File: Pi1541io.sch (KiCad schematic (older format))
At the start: 19 parts, among them J1 IEC, J2 IEC2, J3 ExtSpkr, P1 Conn_02x20_Odd_Even, SW1 SW_Push, SW2 SW_Push, SW3 SW_Push, SW4 SW_Push, SW5 SW_Push, U1 LevelShifter

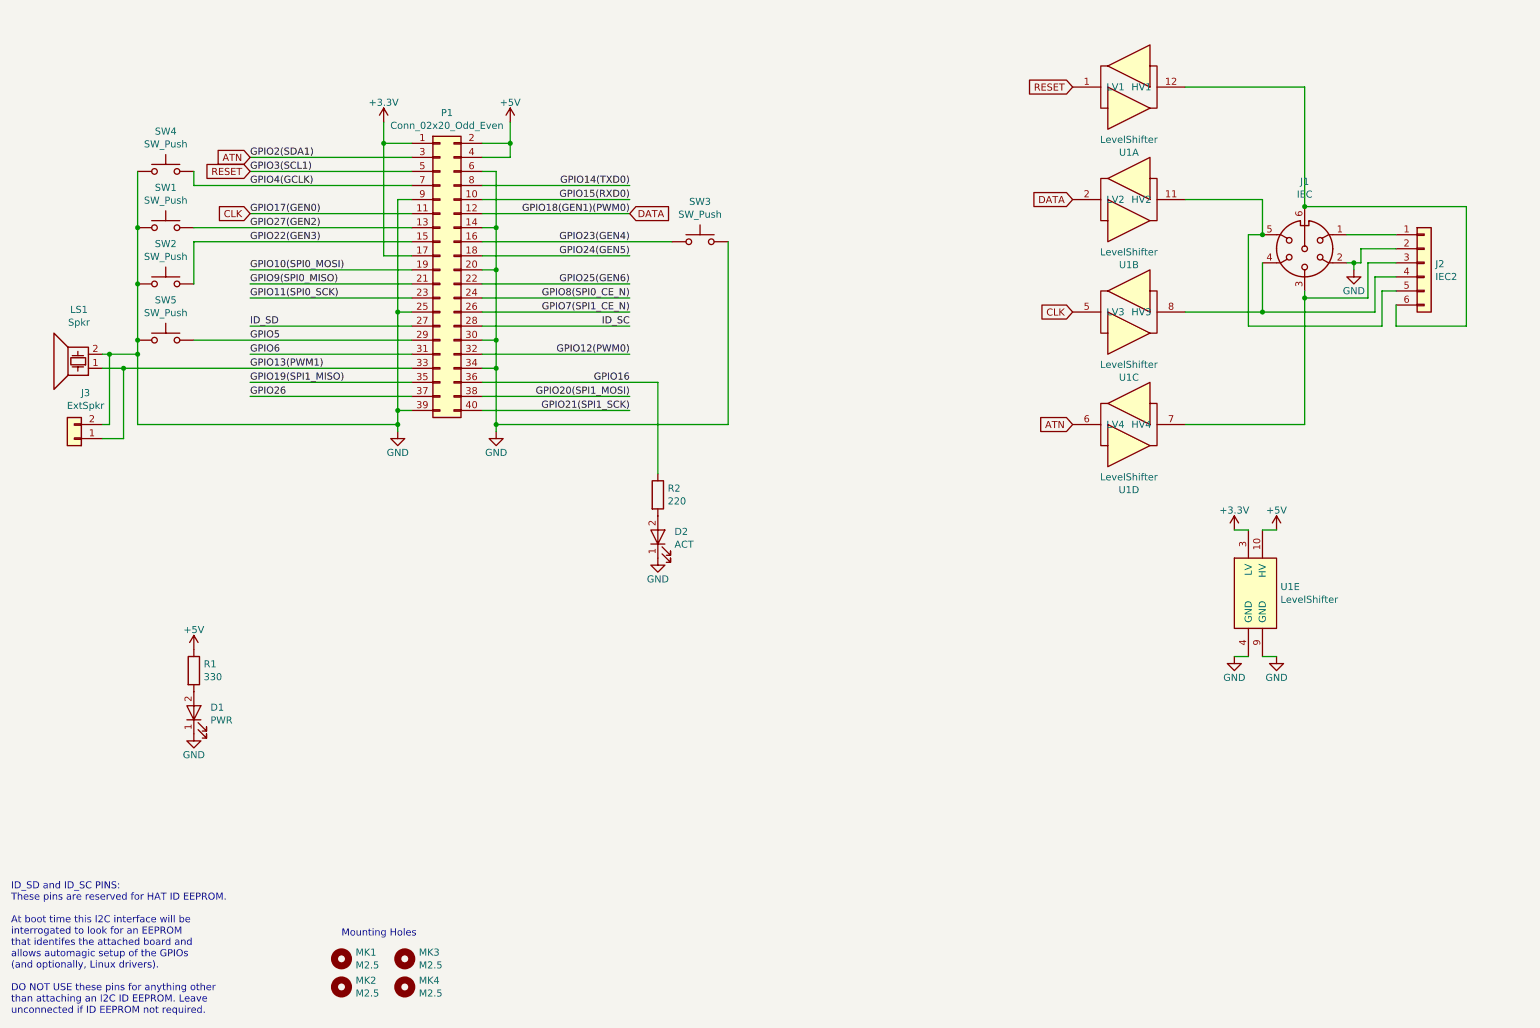
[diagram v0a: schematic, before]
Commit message: Added second IEC port and reset button.
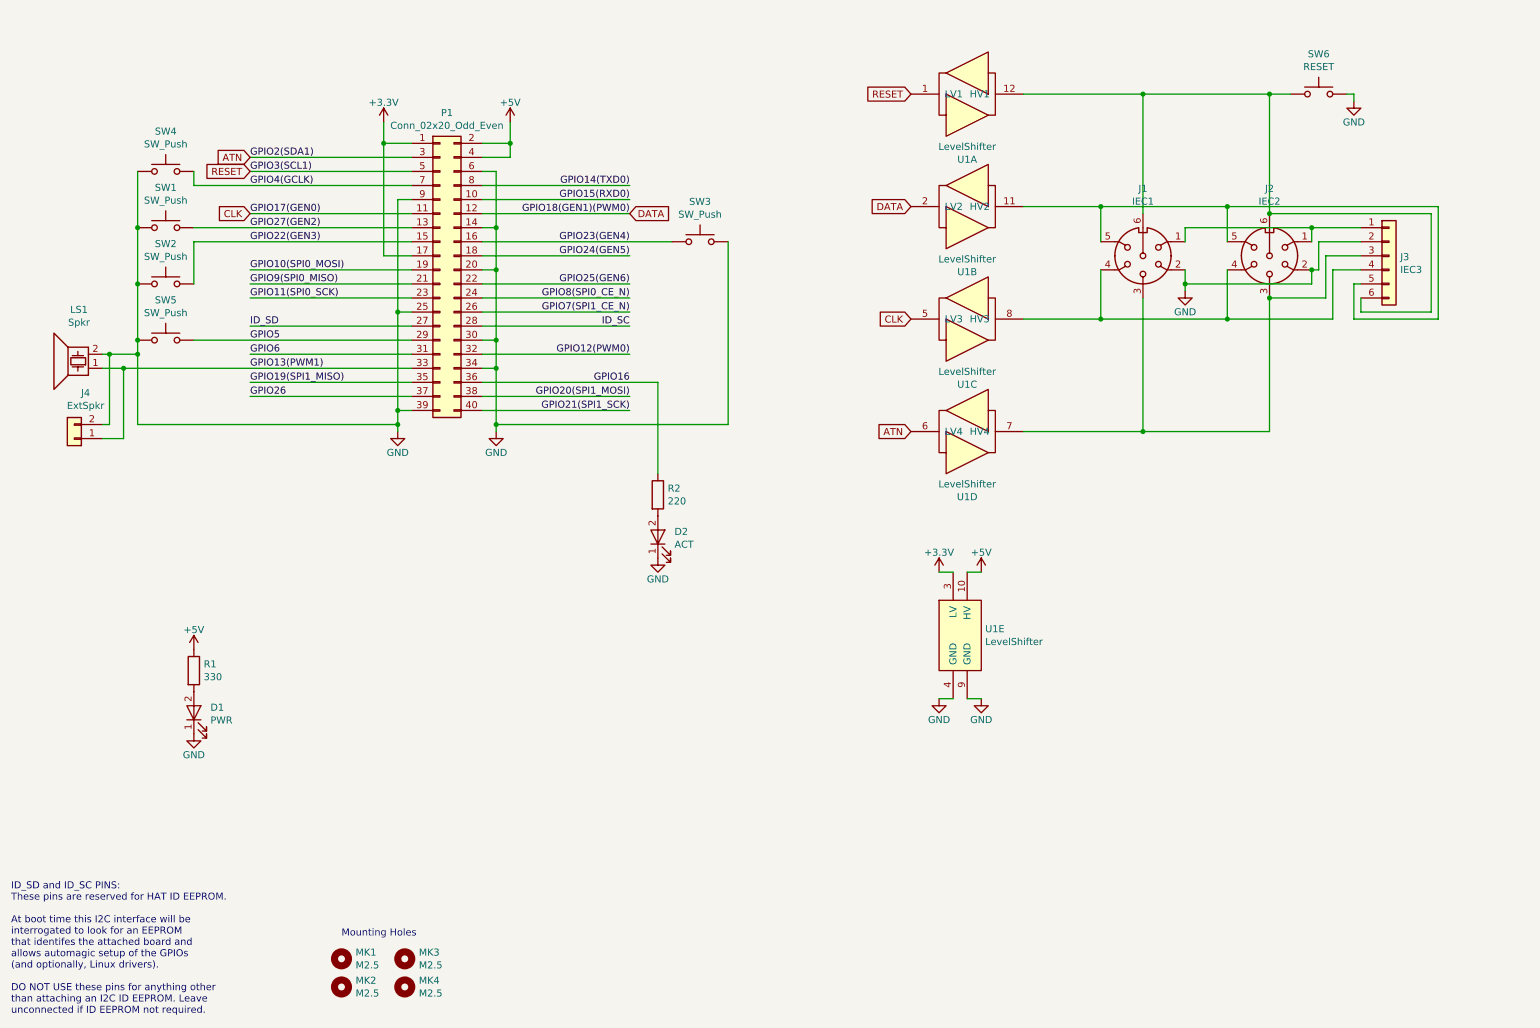
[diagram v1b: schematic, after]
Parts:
- added J2: IEC2, DIN-Connector:DIN-6, symbol Connector:DIN-6
- added SW6: RESET, Buttons_Switches_THT:SW_PUSH_6mm, symbol Switch:SW_Push
- J1: value IEC -> IEC1
- J3: renamed from J2; value IEC2 -> IEC3
- renumbered J3 to J4
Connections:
- net GND: now also J2.2, SW6.2
- net at J1.6, J3.6 (Pin_6), U1.12 (HV1): now also J2.6, SW6.1
- net at J1.4, J3.4 (Pin_4), U1.8 (HV3): now also J2.4
- net at J1.3, J3.3 (Pin_3), U1.7 (HV4): now also J2.3
- net at J1.1, J3.1 (Pin_1): now also J2.1
- net at J1.5, J3.5 (Pin_5), U1.11 (HV2): now also J2.5
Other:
- moved on the sheet: J1, J3, U1A, U1B, U1C, U1D, U1E

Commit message: Adding alternate TXS0108 level shifter module to choose from.
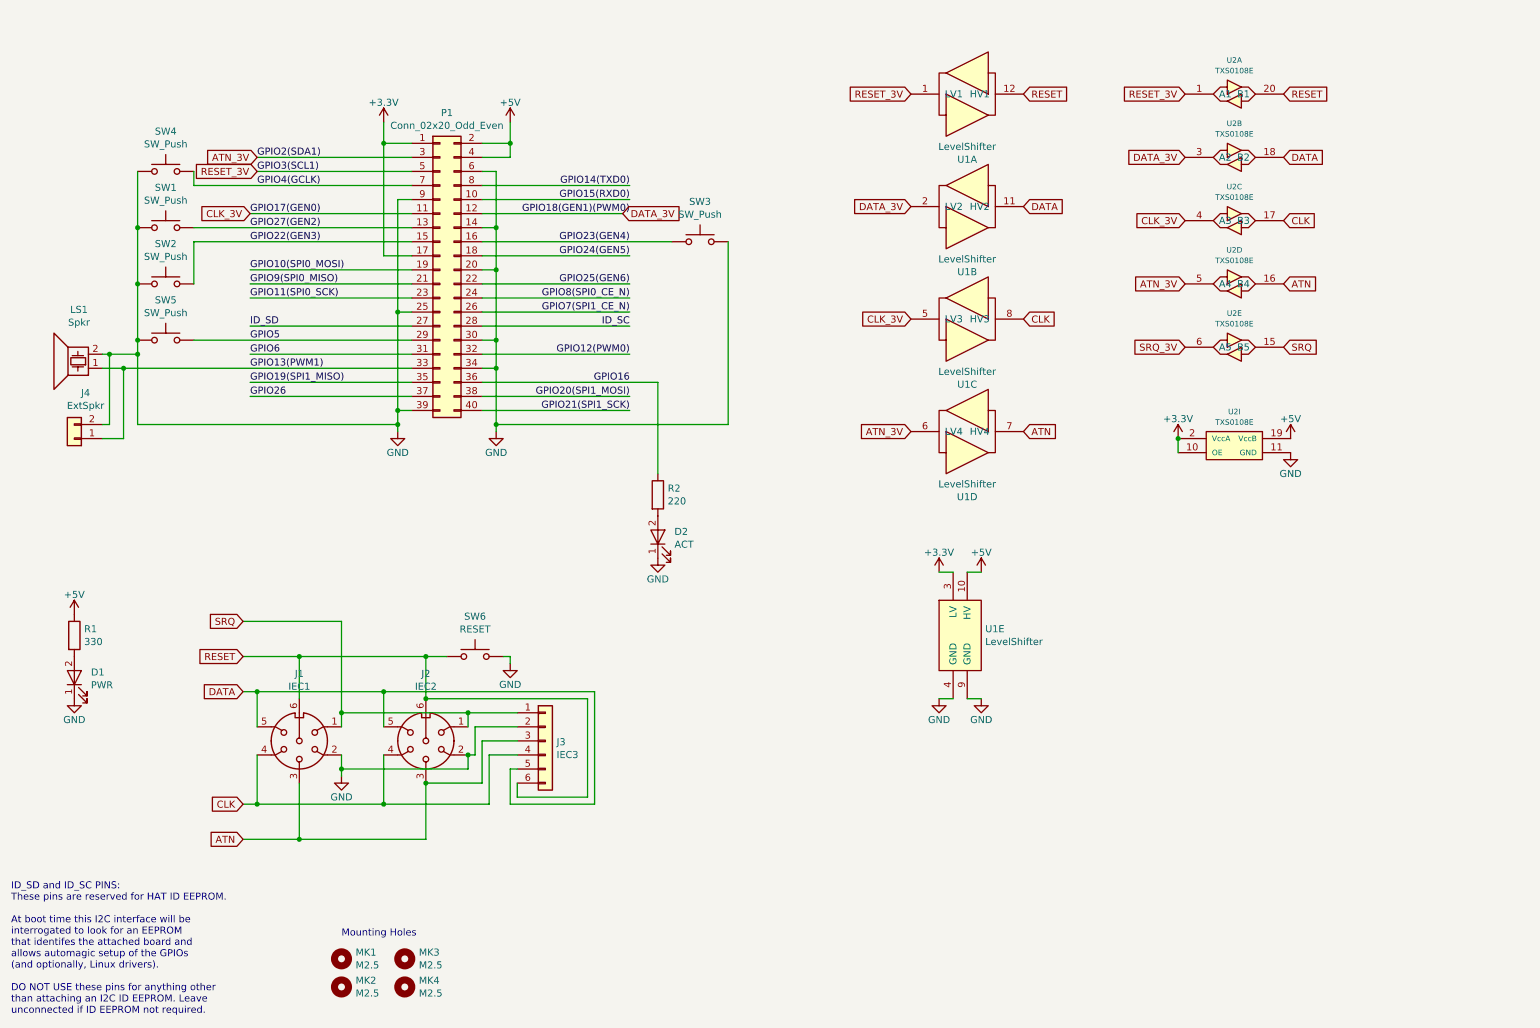
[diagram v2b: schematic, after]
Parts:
- added U2: TXS0108E, symbol hackup:TXS0108E
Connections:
- net +3V3: now also U2.10 (OE), U2.2 (VccA)
- net +5V: now also U2.19 (VccB)
- net ATN: now also J1.3, J2.3, J3.3 (Pin_3), U1.7 (HV4), U2.16 (B4); no longer P1.3 (Pin_3), U1.6 (LV4)
- net CLK: now also J1.4, J2.4, J3.4 (Pin_4), U1.8 (HV3), U2.17 (B3); no longer P1.11 (Pin_11), U1.5 (LV3)
- net DATA: now also J1.5, J2.5, J3.5 (Pin_5), U1.11 (HV2), U2.18 (B2); no longer P1.12 (Pin_12), U1.2 (LV2)
- net GND: now also U2.11 (GND)
- net RESET: now also J1.6, J2.6, J3.6 (Pin_6), SW6.1, U1.12 (HV1), U2.20 (B1); no longer P1.5 (Pin_5), U1.1 (LV1)
- net SRQ: now reaches J1.1, J2.1, J3.1 (Pin_1)
- net SRQ: now also U2.15 (B5)
- new net ATN_3V: P1.3 (Pin_3), U1.6 (LV4), U2.5 (A4)
- new net CLK_3V: P1.11 (Pin_11), U1.5 (LV3), U2.4 (A3)
- new net DATA_3V: P1.12 (Pin_12), U1.2 (LV2), U2.3 (A2)
- new net RESET_3V: P1.5 (Pin_5), U1.1 (LV1), U2.1 (A1)
- new net SRQ_3V: U2.6 (A5)
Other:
- moved on the sheet: D1, J1, J2, J3, R1, SW6

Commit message: Adding alternate TXS0108 level shifter module to choose from.
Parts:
- U2: footprint (none) -> hackup:TXS0108Module
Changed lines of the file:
@@
 F 0 "U2" H 9350 1291 39  0000 C CNN
 F 1 "TXS0108E" H 9350 1216 39  0000 C CNN
-F 2 "" H 9350 1050 50  0001 C CNN
+F 2 "hackup:TXS0108Module" H 9350 1050 50  0001 C CNN
 F 3 "" H 9350 1050 50  0001 C CNN
 	1    9350 1050
@@
 F 0 "U2" H 9350 1741 39  0000 C CNN
 F 1 "TXS0108E" H 9350 1666 39  0000 C CNN
-F 2 "" H 9350 1500 50  0001 C CNN
+F 2 "hackup:TXS0108Module" H 9350 1500 50  0001 C CNN
 F 3 "" H 9350 1500 50  0001 C CNN
 	2    9350 1500
@@
 F 0 "U2" H 9350 2191 39  0000 C CNN
 F 1 "TXS0108E" H 9350 2116 39  0000 C CNN
-F 2 "" H 9350 1950 50  0001 C CNN
+F 2 "hackup:TXS0108Module" H 9350 1950 50  0001 C CNN
 F 3 "" H 9350 1950 50  0001 C CNN
 	3    9350 1950
@@
 F 0 "U2" H 9350 2641 39  0000 C CNN
 F 1 "TXS0108E" H 9350 2566 39  0000 C CNN
-F 2 "" H 9350 2400 50  0001 C CNN
+F 2 "hackup:TXS0108Module" H 9350 2400 50  0001 C CNN
 F 3 "" H 9350 2400 50  0001 C CNN
 	4    9350 2400
@@
 F 0 "U2" H 9350 3091 39  0000 C CNN
 F 1 "TXS0108E" H 9350 3016 39  0000 C CNN
-F 2 "" H 9350 2850 50  0001 C CNN
+F 2 "hackup:TXS0108Module" H 9350 2850 50  0001 C CNN
 F 3 "" H 9350 2850 50  0001 C CNN
 	5    9350 2850
@@
 F 0 "U2" H 9350 3791 39  0000 C CNN
 F 1 "TXS0108E" H 9350 3716 39  0000 C CNN
-F 2 "" H 9350 3550 50  0001 C CNN
+F 2 "hackup:TXS0108Module" H 9350 3550 50  0001 C CNN
 F 3 "" H 9350 3550 50  0001 C CNN
 	9    9350 3550
@@
 $EndComp
 $Comp
-L power:GND #PWR?
+L power:GND #PWR0110
 U 1 1 5B06D334
 P 9750 3600
-F 0 "#PWR?" H 9750 3350 50  0001 C CNN
+F 0 "#PWR0110" H 9750 3350 50  0001 C CNN
 F 1 "GND" H 9750 3450 50  0000 C CNN
 F 2 "" H 9750 3600 50  0000 C CNN
@@
 $EndComp
 $Comp
-L power:+5V #PWR?
+L power:+5V #PWR0111
 U 1 1 5B06D37D
 P 9750 3500
-F 0 "#PWR?" H 9750 3350 50  0001 C CNN
+F 0 "#PWR0111" H 9750 3350 50  0001 C CNN
 F 1 "+5V" H 9750 3640 50  0000 C CNN
 F 2 "" H 9750 3500 50  0000 C CNN
@@
 $EndComp
 $Comp
-L power:+3.3V #PWR?
+L power:+3.3V #PWR0112
 U 1 1 5B06D3C6
 P 8950 3500
-F 0 "#PWR?" H 8950 3350 50  0001 C CNN
+F 0 "#PWR0112" H 8950 3350 50  0001 C CNN
 F 1 "+3.3V" H 8950 3640 50  0000 C CNN
 F 2 "" H 8950 3500 50  0000 C CNN

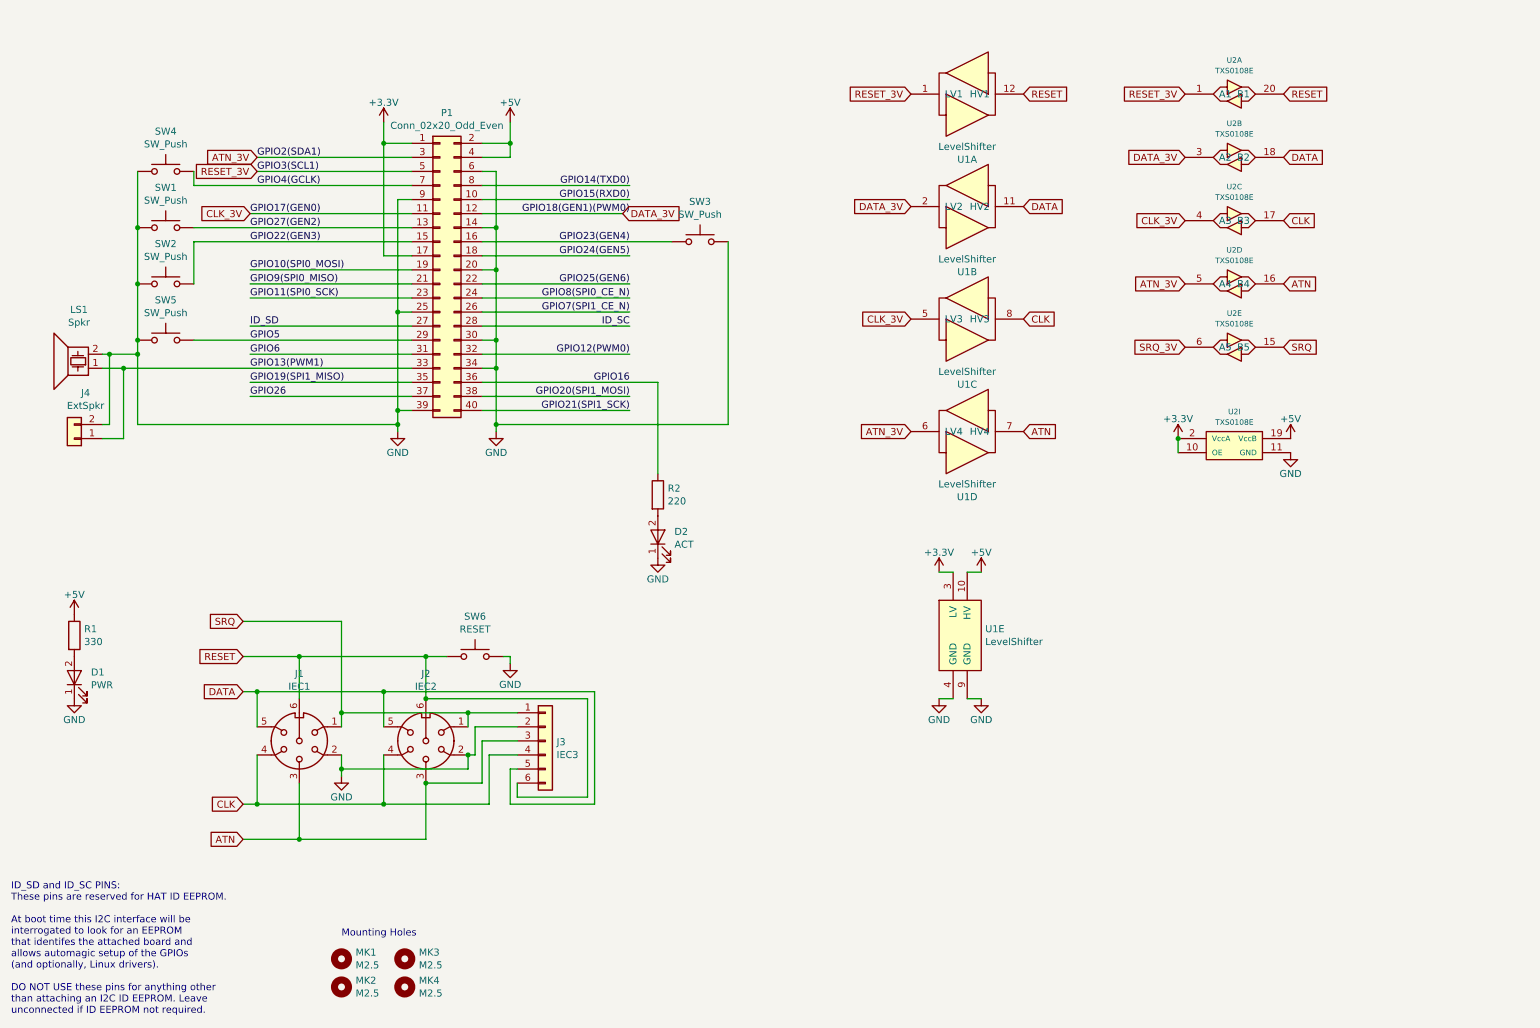
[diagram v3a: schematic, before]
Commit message: Reserved SRQ pin.
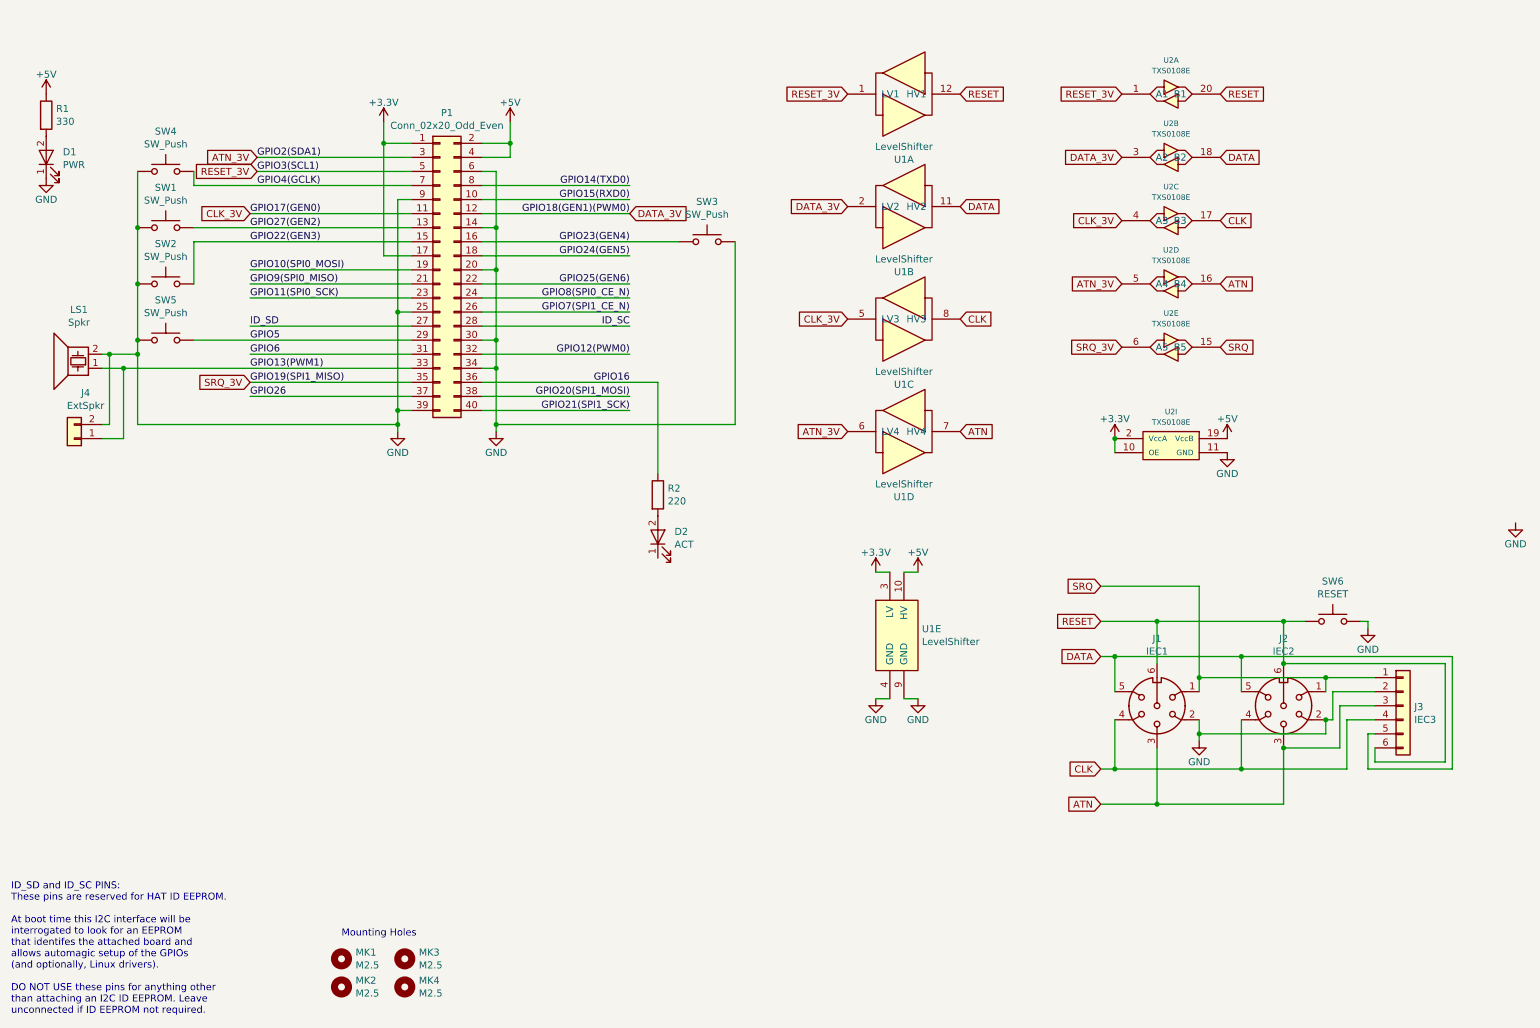
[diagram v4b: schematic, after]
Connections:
- net GPIO19(SPI1_MISO) is gone; now on net SRQ_3V: P1.35 (Pin_35)
- net GND: no longer D2.1 (K)
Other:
- moved on the sheet: D1, J1, J2, J3, R1, SW3, SW6, U1A, U1B, U1C, U1D, U1E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

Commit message: Fix.
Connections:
- net GND: now also D2.1 (K)
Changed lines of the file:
@@
 L power:GND #PWR0108
 U 1 1 5AF39D39
-P 11350 4100
-F 0 "#PWR0108" H 11350 3850 50  0001 C CNN
-F 1 "GND" H 11350 3950 50  0000 C CNN
-F 2 "" H 11350 4100 50  0000 C CNN
-F 3 "" H 11350 4100 50  0000 C CNN
-	1    11350 4100
+P 5250 4350
+F 0 "#PWR0108" H 5250 4100 50  0001 C CNN
+F 1 "GND" H 5250 4200 50  0000 C CNN
+F 2 "" H 5250 4350 50  0000 C CNN
+F 3 "" H 5250 4350 50  0000 C CNN
+	1    5250 4350
 	1    0    0    -1
 $EndComp
